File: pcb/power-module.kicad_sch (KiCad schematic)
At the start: 36 parts, among them J1 USB_C_PowerOnly_6P, J2 Power, U1 AZ1084-3.3, U2 LM66200DRLR

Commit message: revamped using different examples
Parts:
- C7: JLCPCB C3339 -> (none)
- L1: JLCPCB C408335 -> (none)

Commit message: Updated parameters on some parts
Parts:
- C2, C3, C4, C5, C6: MN (none) -> Samsung
- C7: MN (none) -> Honor Elec; MPN (none) -> RVT1V101M0607
- J2: Digikey (none) -> 455-SM04B-SRSS-TBTR-ND; Mouser (none) -> 306-SM04BSRSSTBLFSN
- R1, R2: Digikey (none) -> 541-5.1KGTR-ND; MN (none) -> FOJAN; Mouser (none) -> 71-CRCW0603J-5.1K-E3

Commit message: Added panelization; cleaned up
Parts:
- C7: FT Rotation Offset (none) -> 180
- D3, D4: footprint LED_SMD:LED_0603_1608Metric -> CRGM Passive:LED_0603_1608Metric
- U1: FT Position Offset (none) -> -3.3,0
- U2: FT Rotation Offset (none) -> -90
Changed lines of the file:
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@@
 			)
 		)
+		(property "FT Rotation Offset" "180"
+			(at 135.89 86.36 0)
+			(effects
+				(font
+					(size 1.27 1.27)
+				)
+				(hide yes)
+			)
+		)
 		(pin "1"
 		)
@@
 			)
 		)
-		(property "Footprint" "LED_SMD:LED_0603_1608Metric"
+		(property "Footprint" "CRGM Passive:LED_0603_1608Metric"
 			(at 163.83 186.69 0)
 			(effects
@@
 			)
 		)
+		(property "FT Position Offset" "-3.3,0"
+			(at 31.75 120.65 0)
+			(effects
+				(font
+					(size 1.27 1.27)
+				)
+				(hide yes)
+			)
+		)
 		(pin "3"
 		)
@@
 			)
 		)
-		(property "Footprint" "LED_SMD:LED_0603_1608Metric"
+		(property "Footprint" "CRGM Passive:LED_0603_1608Metric"
 			(at 147.32 186.69 0)
 			(effects
@@
 				(hide yes)
 			)
+		)
+		(property "FT Rotation Offset" "-90"
+			(at 49.53 80.01 0)
+			(effects
+				(font
+					(size 1.27 1.27)
+				)
+				(hide yes)
+			)

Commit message: alternate inductor - primary is out of stock
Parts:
- L1: LCSC C408335 -> C438930
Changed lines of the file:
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@@
 			)
 		)
-		(property "LCSC" "C408335"
+		(property "LCSC" "C438930"
 			(at 114.3 78.74 0)
 			(effects

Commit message: Part swap; moved from 2x2 panel to 1x2 panel
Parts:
- L1: MN Sunlord -> Cybermax; MPN MWSA0402S-2R2MT -> CMLO0420H2R2MTT
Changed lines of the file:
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@@
 			)
 		)
-		(property "Datasheet" "https://jlcpcb.com/api/file/downloadByFileSystemAccessId/8552174640249257984"
+		(property "Datasheet" "https://jlcpcb.com/api/file/downloadByFileSystemAccessId/8588935518867869696"
 			(at 114.3 78.74 0)
 			(effects
@@
 			)
 		)
-		(property "Description" "4.5A 2.2uH ±20% 5A SMD,4.4x4.2mm Power Inductors"
+		(property "Description" "3A 2.2uH Shielded inductor ±20% SMD,4.4x4.2mm Power Inductors"
 			(at 114.3 78.74 0)
 			(effects
@@
 			)
 		)
-		(property "MN" "Sunlord"
+		(property "MN" "Cybermax"
 			(at 114.3 78.74 90)
 			(effects
@@
 			)
 		)
-		(property "MPN" "MWSA0402S-2R2MT"
+		(property "MPN" "CMLO0420H2R2MTT"
 			(at 114.3 78.74 90)
 			(effects

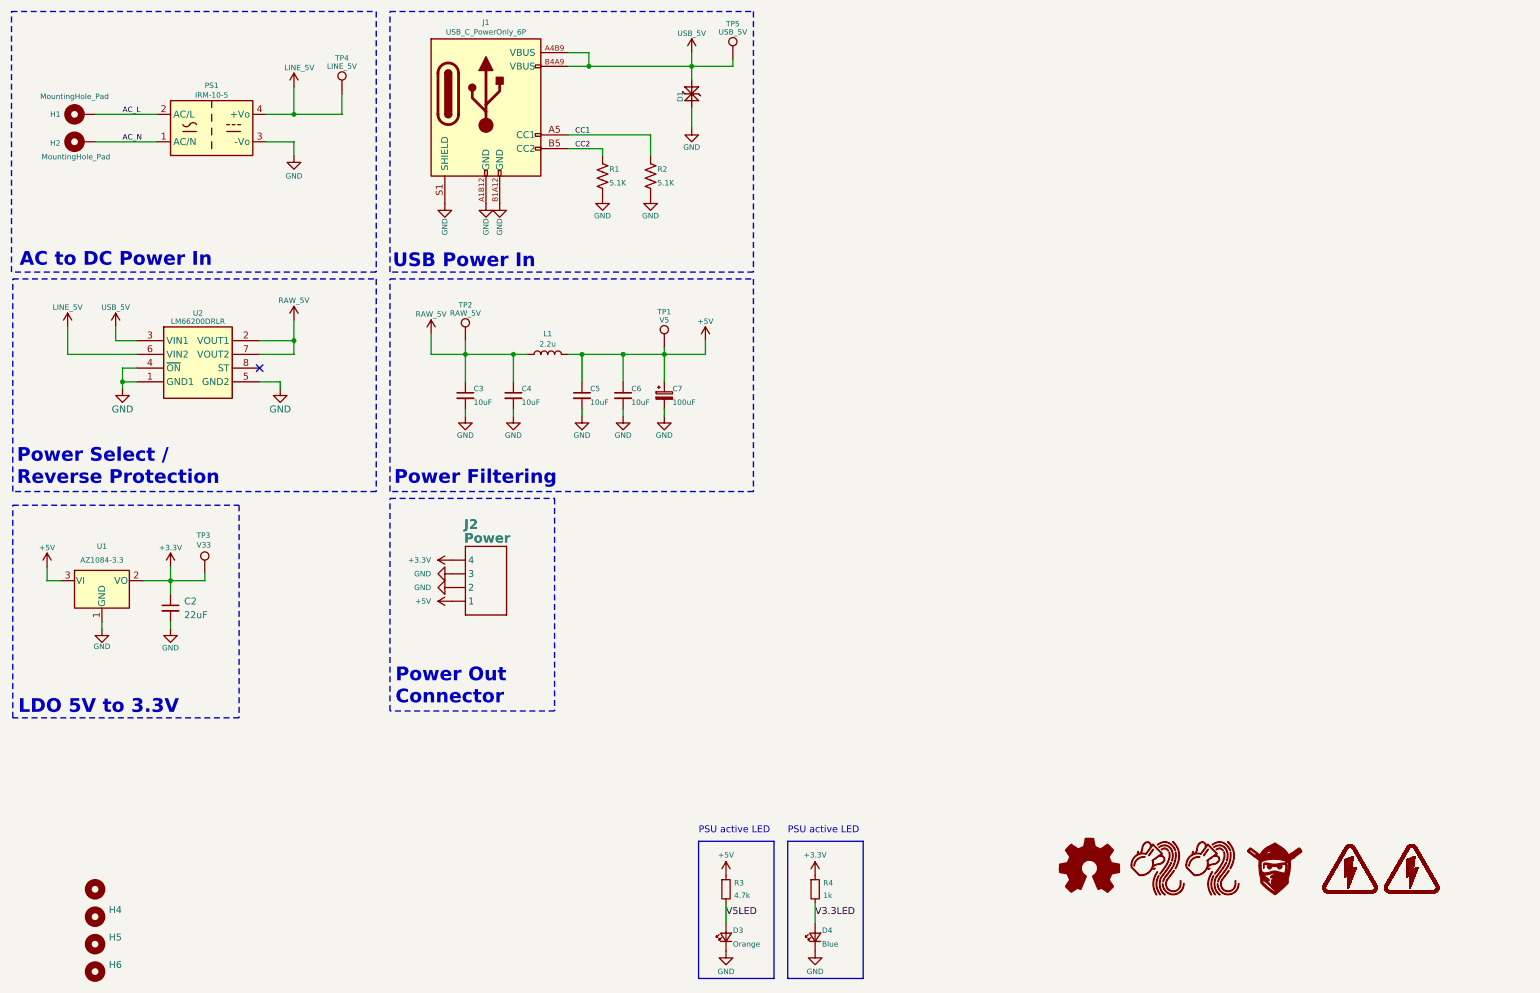
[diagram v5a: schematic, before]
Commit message: Separated 22uF into two 10uF; rerouted everything for better layout
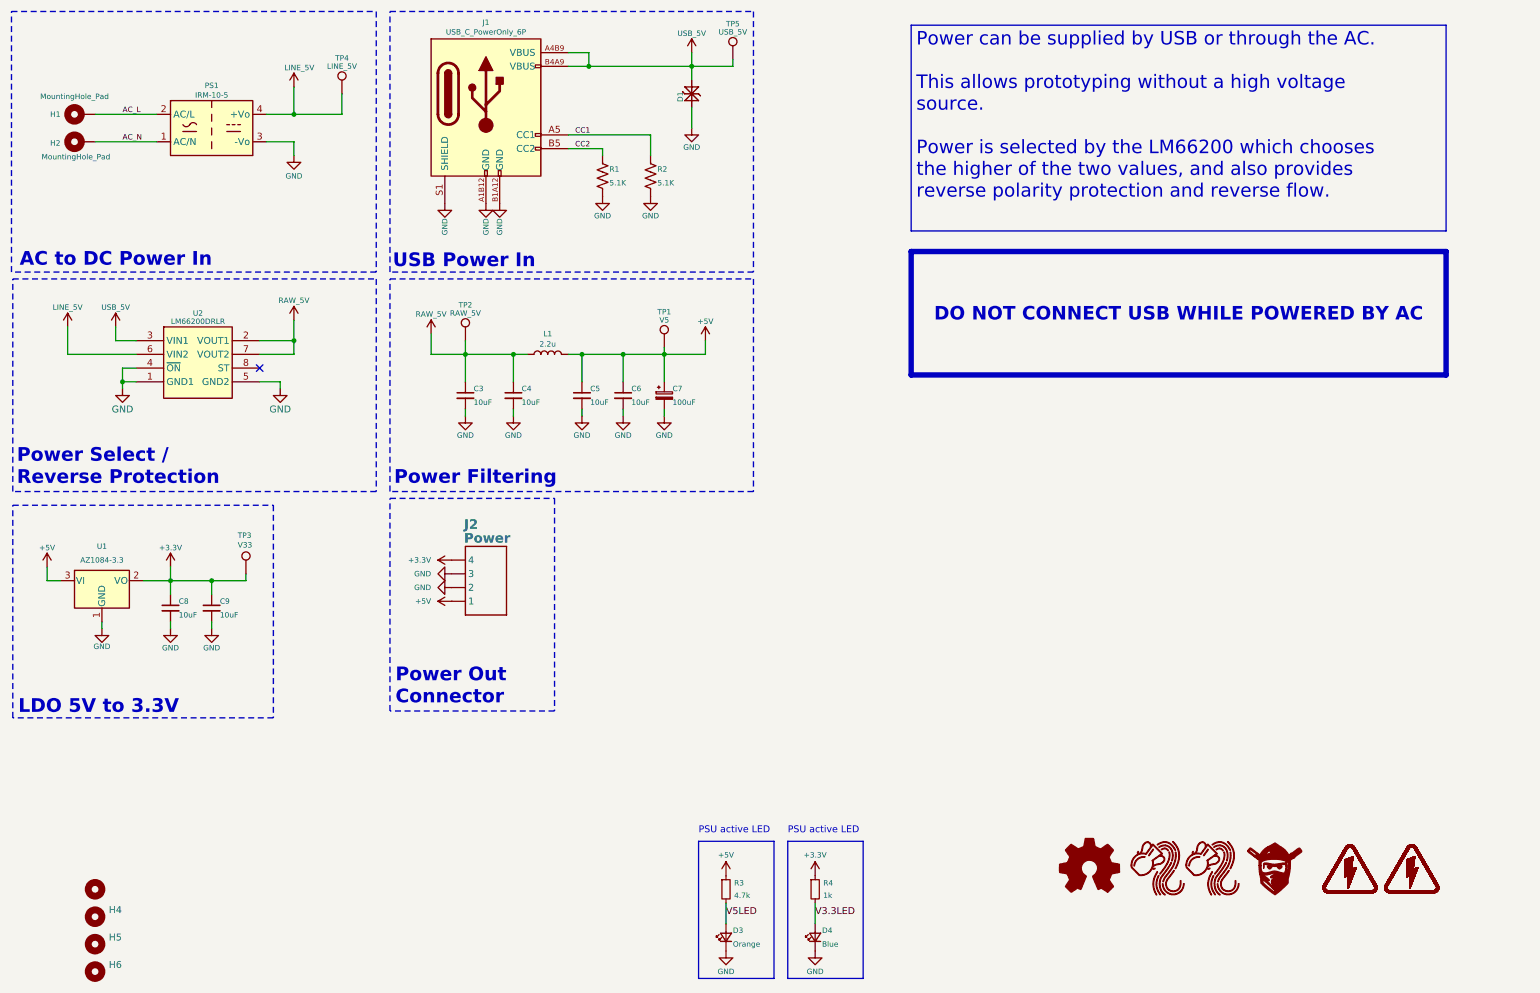
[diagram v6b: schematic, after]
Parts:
- removed C2: 22uF, Capacitor_SMD:C_0603_1608Metric, symbol Device:C_Small
- added C8, C9: 10uF, Capacitor_SMD:C_0603_1608Metric, symbol Device:C_Small
- U1: FT Position Offset -3.3,0 -> (none)
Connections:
- net +3.3V: now also C8.1, C9.1
- net GND: now also C8.2, C9.2
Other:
- moved on the sheet: TP3
